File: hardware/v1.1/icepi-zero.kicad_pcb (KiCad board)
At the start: 4 copper layers, 65 x 30 mm, 144 parts, among them J1 Conn_02x20_Counter_Clockwise, J2 HDMI_C_1.3, J3 USB_C_Receptacle_USB2.0_14P, J4 USB_C_Receptacle_USB2.0_14P, J5 USB_C_Receptacle_USB2.0_14P, J6 Micro_SD_Card_Det2, SW1 SW_Push, SW2 SW_Push, U1 ECP5U_25F_CABGA256, U10 W9825G6KH, U11 W25Q128JVS, U2 TLV62569DBV, U3 TLV62569DBV, U4 TLV62569DBV, U5 PCA9306DC1, U6 FT231XQ, U7 TPD2EUSB30A, U8 TPD2EUSB30A, U9 TPD2EUSB30A, Y1 SITxxxxxx-1x-33E-50.000000

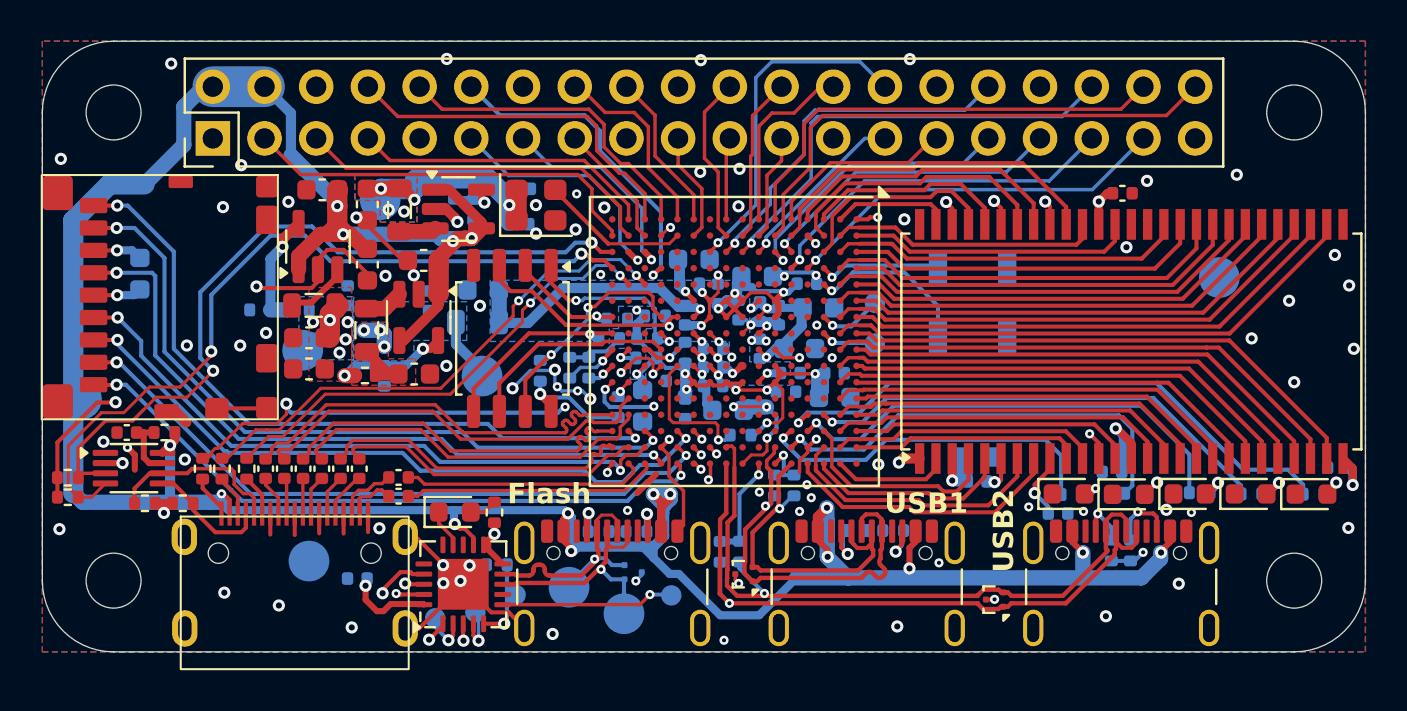
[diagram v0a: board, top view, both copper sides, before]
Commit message: Fix typo in filename
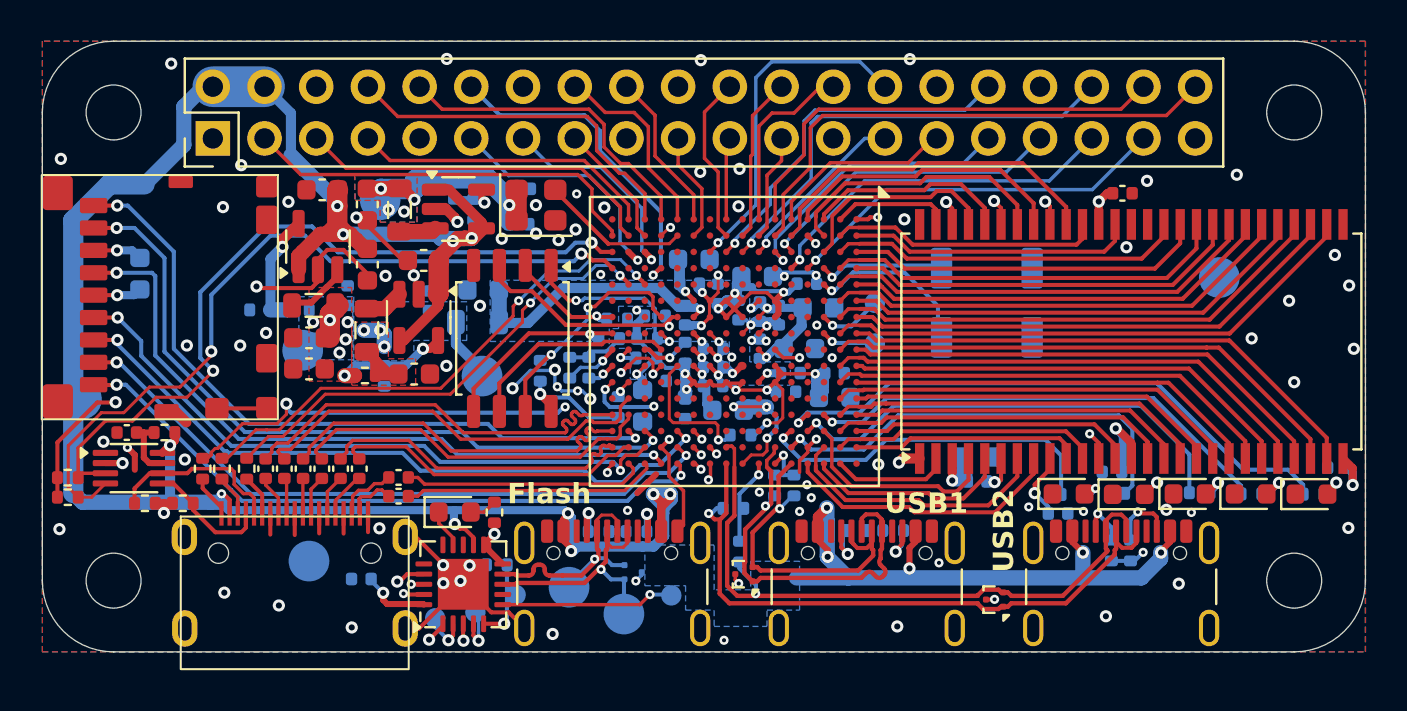
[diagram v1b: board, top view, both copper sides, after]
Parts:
- SW1, SW2: footprint Button_Switch_SMD:SW_SPST_B3U-1000P -> icepi-lib:switch_button_TS-1088-AR02016
- moved LOGO1 10.6 mm to (168.6, 103.5)
- moved R41 2.23 mm to (149.9, 113.0), turned to 180 degrees
- moved SW2 0.71 mm to (162.4, 104.5)
- moved SW1 0.70 mm to (162.4, 101.2)
- moved C38 0.20 mm to (131.7, 116.4)
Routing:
- net +5V: track 183.5 -> 173.2 mm
- net USB_TXD: track 23.4 -> 22.3 mm
- net USB3_PULL: track 5.15 -> 4.21 mm
- net Net-(U6-3V3OUT): track 13.8 -> 13.0 mm
- net ~{USB_RTS}: track 20.8 -> 20.1 mm
- net D3+: track 33.1 -> 32.4 mm
- net ~{USB_DTR}: track 20.5 -> 19.8 mm
- net GND: vias 109 -> 111
- added copper zone on B.Cu, net +5V
